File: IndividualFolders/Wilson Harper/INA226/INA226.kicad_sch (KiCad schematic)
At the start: 6 parts, among them U1 INA226

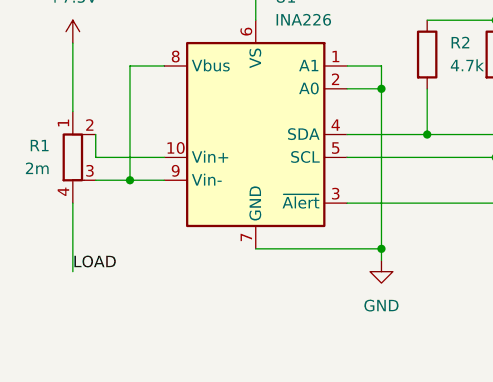
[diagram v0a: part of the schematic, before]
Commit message: Update INA226 schematic
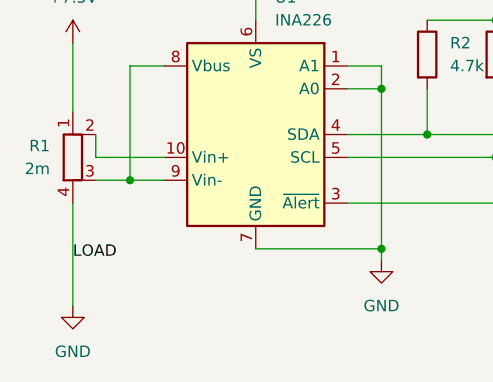
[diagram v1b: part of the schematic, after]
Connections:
- net LOAD is gone; now on net GND: R1.4
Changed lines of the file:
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@@
-	(wire
-		(pts
-			(xy 124.46 86.36) (xy 124.46 93.98)
-		)
-		(stroke
-			(width 0)
-			(type default)
-		)
-	)
 	(wire
 		(pts
@@
 		(pts
 			(xy 154.94 78.74) (xy 163.83 78.74)
+		)
+		(stroke
+			(width 0)
+			(type default)
+		)
+	)
+	(wire
+		(pts
+			(xy 124.46 86.36) (xy 124.46 97.79)
 		)
 		(stroke
@@
 		)
 	)
-	(label "LOAD"
-		(at 124.46 93.98 0)
-		(effects
-			(font
-				(size 1.27 1.27)
-			)
-			(justify left bottom)
-		)
-	)
 	(label "Alert"
 		(at 185.42 86.36 0)
@@
 	(label "I2C SDA"
 		(at 185.42 78.74 0)
+		(effects
+			(font
+				(size 1.27 1.27)
+			)
+			(justify left bottom)
+		)
+	)
+	(label "LOAD"
+		(at 124.46 92.71 0)
 		(effects
 			(font
@@
 					(unit 1)
 				)
+			)
+		)
+	)
+	(symbol
+		(lib_id "power:GND")
+		(at 124.46 97.79 0)
+		(unit 1)
+		(exclude_from_sim no)
+		(in_bom yes)
+		(on_board yes)
+		(dnp no)
+		(fields_autoplaced yes)
+		(property "Reference" "#PWR05"
+			(at 124.46 104.14 0)
+			(effects
+				(font
+					(size 1.27 1.27)
+				)
+				(hide yes)
+			)
+		)
+		(property "Value" "GND"
+			(at 124.46 102.87 0)
+			(effects
+				(font
+					(size 1.27 1.27)
+				)
+			)
+		)
+		(property "Footprint" ""
+			(at 124.46 97.79 0)
+			(effects
+				(font
+					(size 1.27 1.27)
+				)
+				(hide yes)
+			)
+		)
+		(property "Datasheet" ""
+			(at 124.46 97.79 0)
+			(effects
+				(font
+					(size 1.27 1.27)
+				)
+				(hide yes)
+			)
+		)
+		(property "Description" "Power symbol creates a global label with name \"GND\" , ground"
+			(at 124.46 97.79 0)
+			(effects
+				(font
+					(size 1.27 1.27)
+				)
+				(hide yes)
+			)
+		)
+		(pin "1"
+		)
+		(instances
+			(project ""
+				(path "/4c57a115-c073-4d7e-bb1c-9e7e194b4904"
+					(reference "#PWR05")
+					(unit 1)
+				)

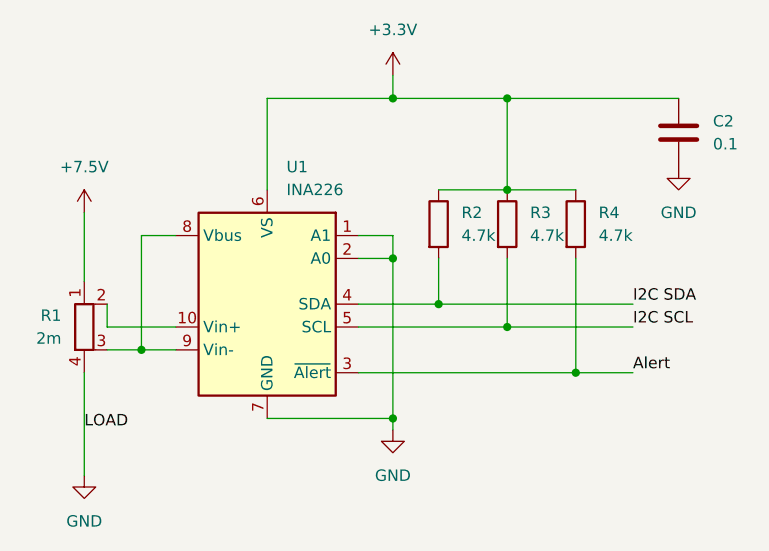
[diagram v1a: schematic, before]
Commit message: Assign footprints
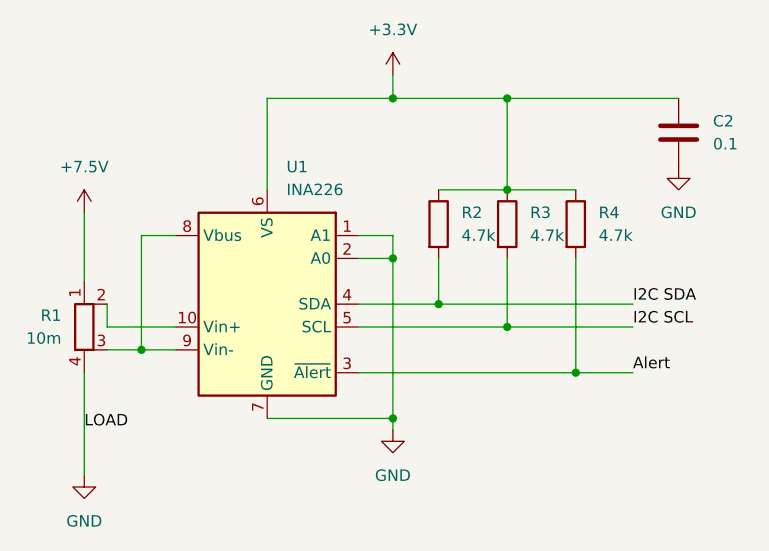
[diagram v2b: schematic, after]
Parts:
- C2: footprint (none) -> Capacitor_SMD:C_0805_2012Metric
- R1: value 2m -> 10m; footprint (none) -> Resistor_SMD:R_2512_6332Metric
- R2, R3, R4: footprint (none) -> Resistor_SMD:R_0805_2012Metric
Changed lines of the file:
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@@
 			)
 		)
-		(property "Value" "2m"
+		(property "Value" "10m"
 			(at 121.92 82.5499 0)
 			(effects
@@
 			)
 		)
-		(property "Footprint" ""
+		(property "Footprint" "Resistor_SMD:R_2512_6332Metric"
 			(at 122.682 81.28 90)
 			(effects
@@
 			)
 		)
-		(property "Footprint" ""
+		(property "Footprint" "Resistor_SMD:R_0805_2012Metric"
 			(at 177.292 69.85 90)
 			(effects
@@
 			)
 		)
-		(property "Footprint" ""
+		(property "Footprint" "Capacitor_SMD:C_0805_2012Metric"
 			(at 191.4652 63.5 0)
 			(effects
@@
 			)
 		)
-		(property "Footprint" ""
+		(property "Footprint" "Resistor_SMD:R_0805_2012Metric"
 			(at 169.672 69.85 90)
 			(effects
@@
 			)
 		)
-		(property "Footprint" ""
+		(property "Footprint" "Resistor_SMD:R_0805_2012Metric"
 			(at 162.052 69.85 90)
 			(effects
